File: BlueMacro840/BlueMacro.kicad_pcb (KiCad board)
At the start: 4 copper layers, 20.3 x 48.3 mm, 33 parts, among them J1 Conn_01x02, J3 USB_C_Receptacle, Q1 SI2301CDS-T1-GE3, U1 TP4054ST, U2 E73-2G4M08S1C, U3 AP2112K-3.3TRG1, U4 Micro, U5 AP2112K-3.3TRG1, Y1 32.768kHz

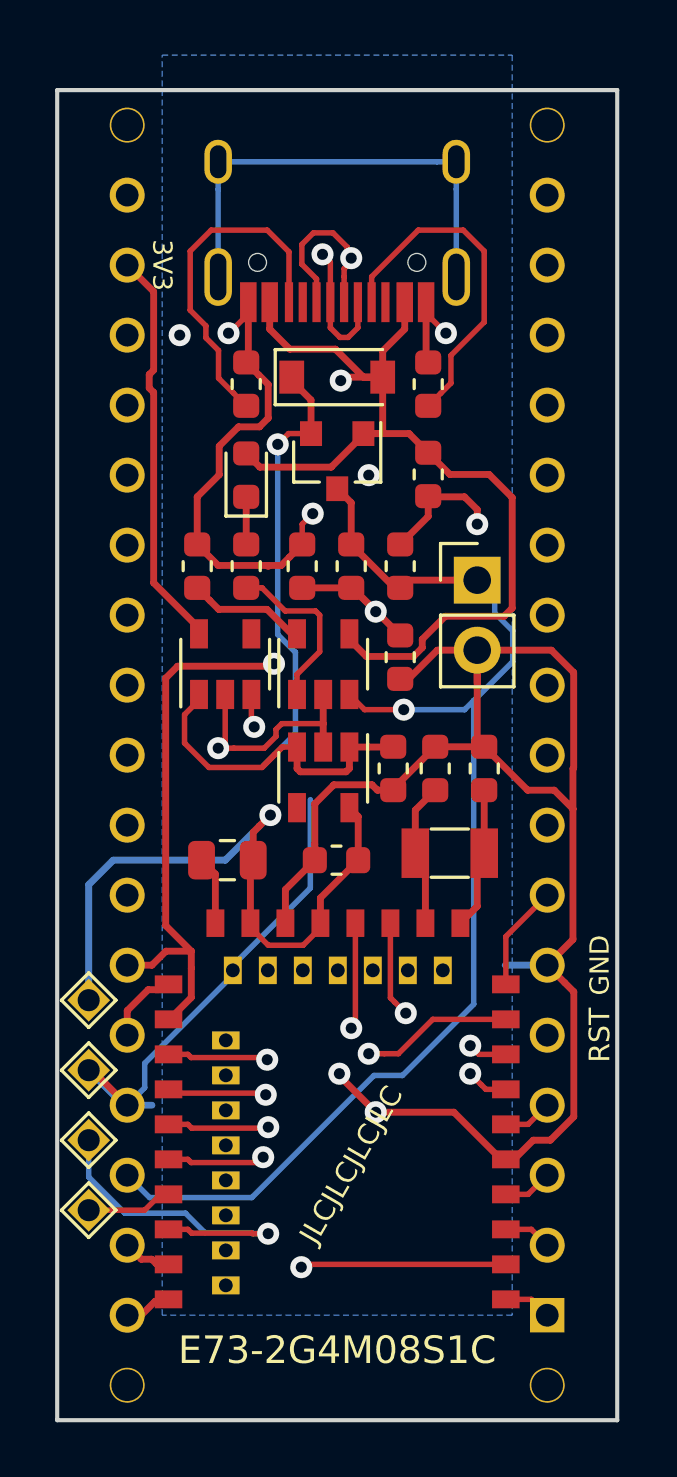
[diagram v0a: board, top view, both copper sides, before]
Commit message: Added BlueMacro PCB. Added Plate PCB.
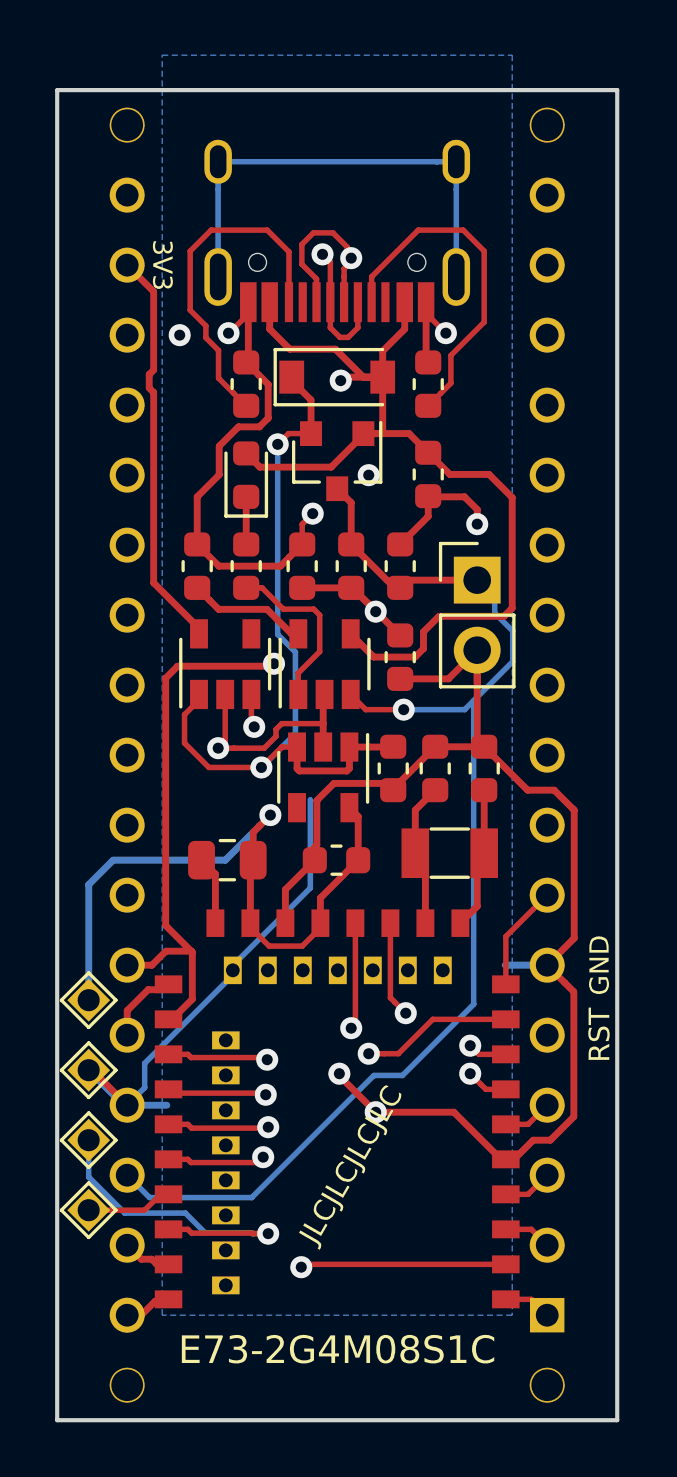
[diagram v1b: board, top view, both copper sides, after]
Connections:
- net /P0.14 renamed /P1.04
- net /P0.18 renamed /P1.10
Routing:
- net GND: track 110.7 -> 102.5 mm
- net Net-(C3-Pad1): track 29.0 -> 28.0 mm, vias 1 -> 2

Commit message: Finished Plate. Fixed errors (missing via, missing solder mask) on BlueMacro
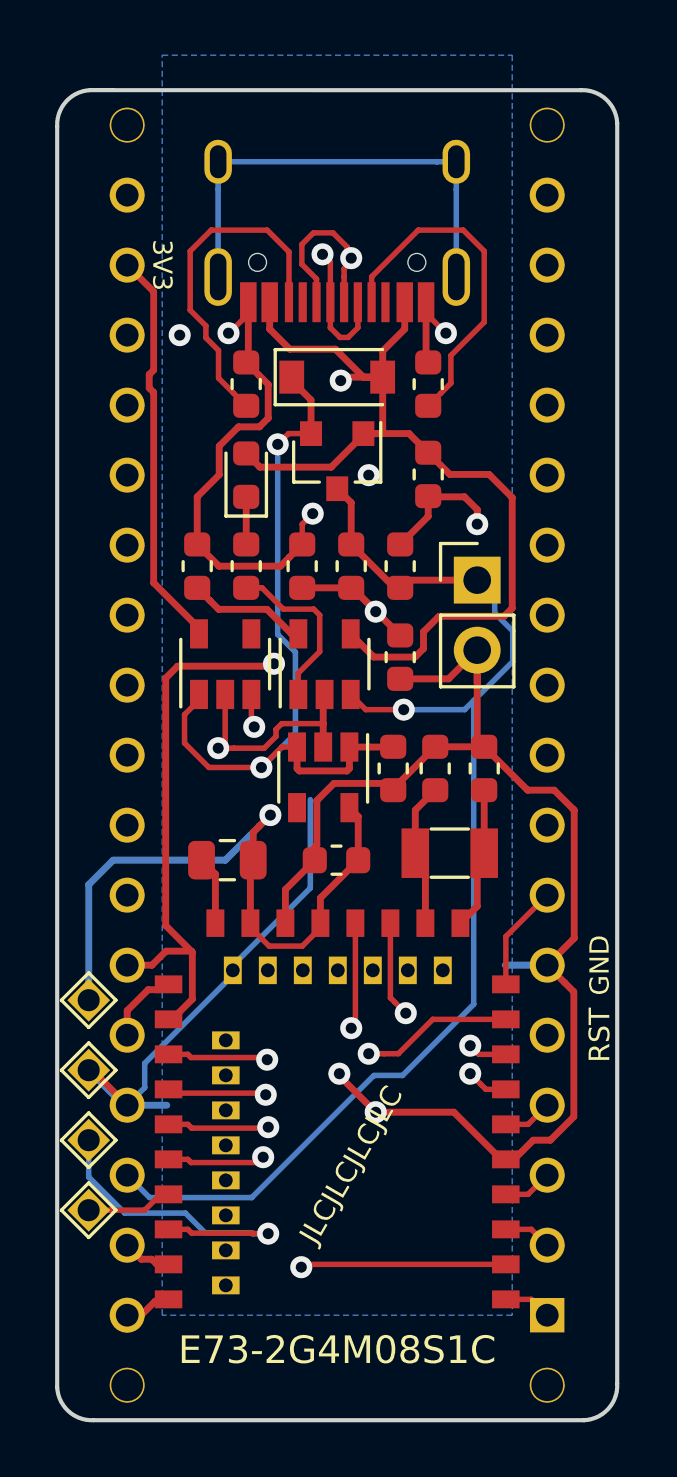
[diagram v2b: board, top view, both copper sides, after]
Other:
- outline, holes or cut-outs redrawn
- board text added: "10"
- board text added: "12"
- board text added: "13"
- board text added: "15"
- board text added: "17"
- board text added: "2"
- board text added: "20"
- board text added: "22"
- board text added: "24"
- board text added: "26"
- board text added: "28"
- board text added: "29"
- board text added: "3"
- board text added: "30"
- board text added: "34"
- board text added: "36"
- board text added: "38"
- board text added: "4"
- board text added: "41"
- board text added: "42"
- board text added: "43"
- board text added: "45"
- board text added: "5"
- board text added: "6"
- board text added: "7"
- board text added: "8"
- board text added: "9"
- board text removed: "0.02"
- board text removed: "0.03"
- board text removed: "0.04"
- board text removed: "0.05"
- board text removed: "0.06"
- board text removed: "0.07"
- board text removed: "0.08"
- board text removed: "0.09"
- board text removed: "0.10"
- board text removed: "0.12"
- board text removed: "0.13"
- board text removed: "0.15"
- board text removed: "0.17"
- board text removed: "0.20"
- board text removed: "0.22"
- board text removed: "0.24"
- board text removed: "0.26"
- board text removed: "0.28"
- board text removed: "0.29"
- board text removed: "0.30"
- board text removed: "1.02"
- board text removed: "1.06"
- board text removed: "1.09"
- board text removed: "1.11"
- board text removed: "1.13"
- board text removed: "NC"
